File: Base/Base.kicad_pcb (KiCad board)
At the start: 2 copper layers, 72.4 x 72.4 mm, 33 parts, among them J1 USB_C_Receptacle_USB2.0_16P, J10 JST_switch_1, J11 JST_switch_2, J12 Conn_touch_1, J13 Conn_touch_2, J2 JST_battery, J3 JST_header, J4 JST_speaker, J5 JST_debug_swd, J6 JST_debug_serial, J7 Conn_speaker_sd, J8 Conn_speaker_gain, J9 Conn_speaker_gnd, SW1 SW_power, U1 MCP73831-2-OT, U2 MAX98357A

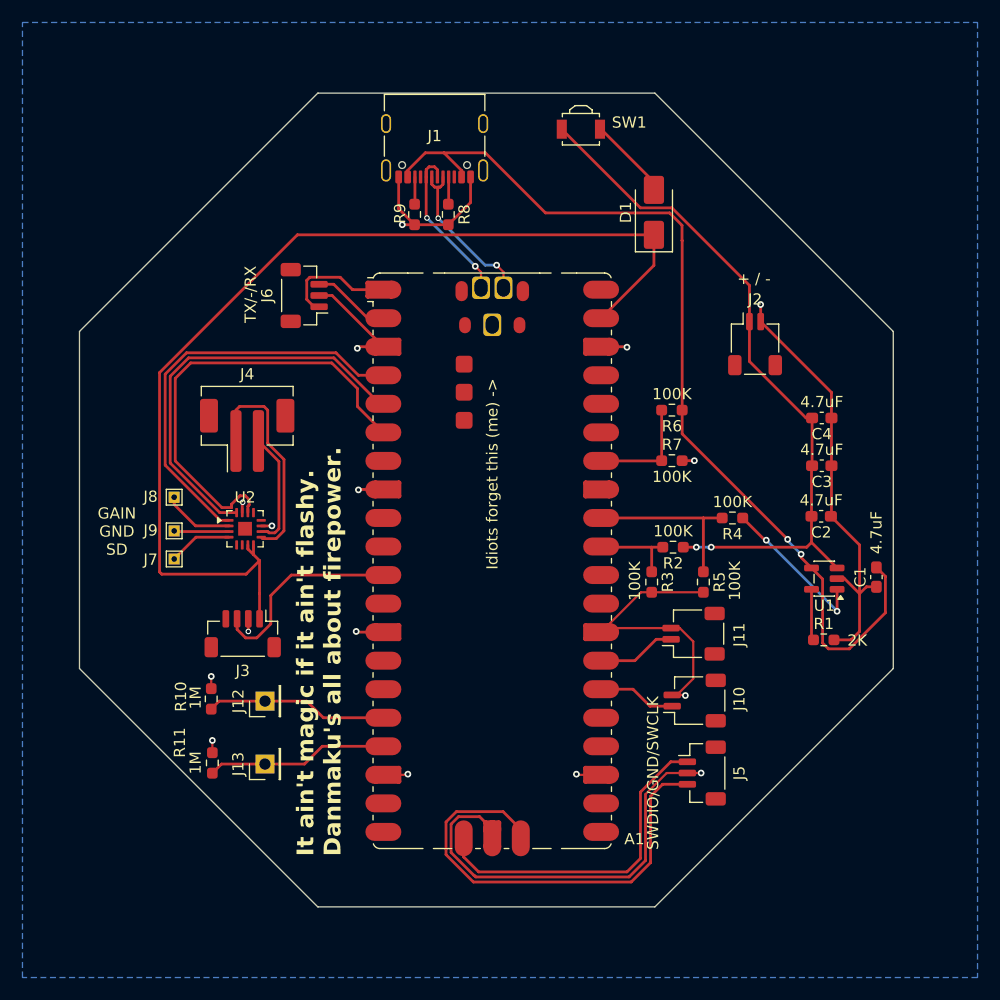
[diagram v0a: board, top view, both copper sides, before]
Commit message: Change switch to JST, fix polarity of battery connector, add power transistors for better LED off capability
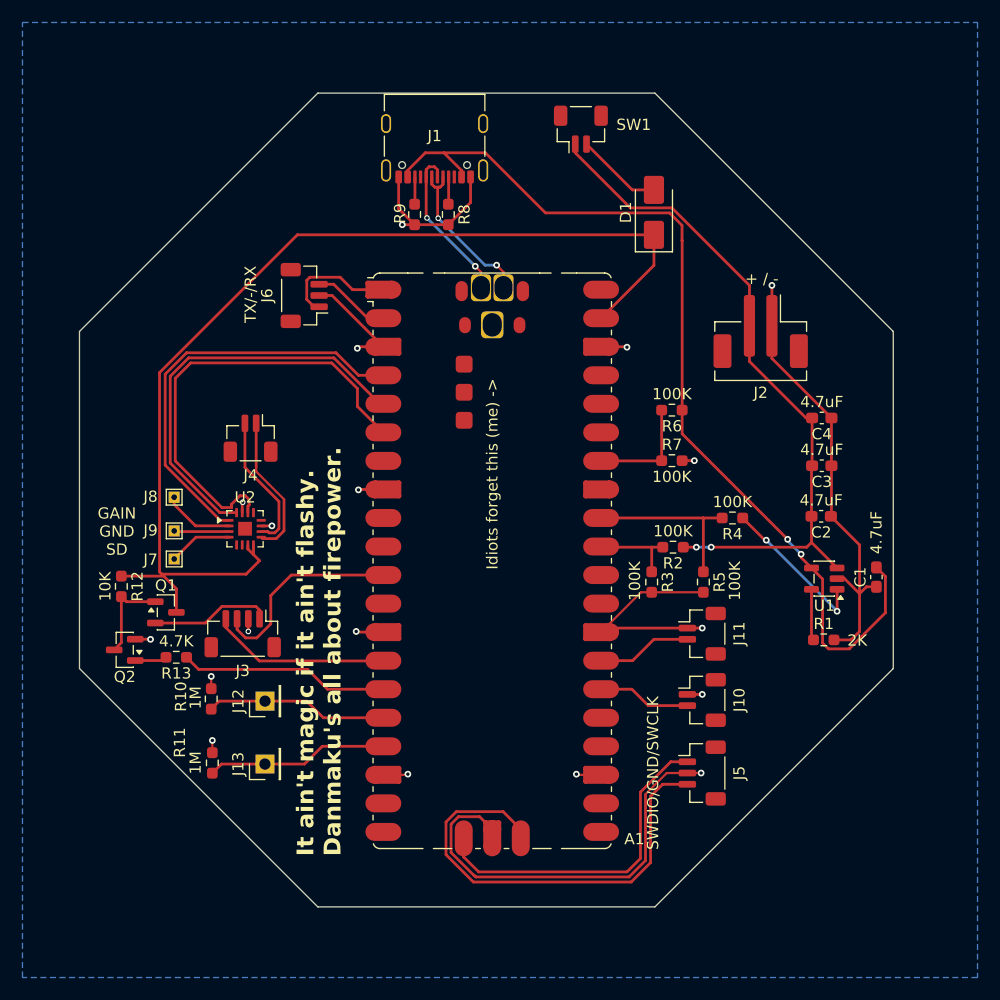
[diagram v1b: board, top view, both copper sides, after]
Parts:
- added Q1: AO3401A, Package_TO_SOT_SMD:SOT-23, F.Cu at (127.8, 112.5)
- added Q2: AO3400A, Package_TO_SOT_SMD:SOT-23, F.Cu at (124.1, 115.8)
- added R12: 10K, Resistor_SMD:R_0603_1608Metric_Pad0.98x0.95mm_HandSolder, F.Cu at (123.8, 110.2)
- added R13: 4.7K, Resistor_SMD:R_0603_1608Metric_Pad0.98x0.95mm_HandSolder, F.Cu at (128.7, 116.5)
- J10, J11: footprint Connector_JST:JST_SH_SM02B-SRSS-TB_1x02-1MP_P1.00mm_Horizontal -> Connector_JST:JST_SH_BM02B-SRSS-TB_1x02-1MP_P1.00mm_Vertical
- J2: footprint Connector_JST:JST_SH_SM02B-SRSS-TB_1x02-1MP_P1.00mm_Horizontal -> Connector_JST:JST_PH_B2B-PH-SM4-TB_1x02-1MP_P2.00mm_Vertical
- J4: footprint Connector_JST:JST_PH_B2B-PH-SM4-TB_1x02-1MP_P2.00mm_Vertical -> Connector_JST:JST_SH_BM02B-SRSS-TB_1x02-1MP_P1.00mm_Vertical
- SW1: footprint Button_Switch_SMD:SW_SPST_B3U-3000P -> Connector_JST:JST_SH_BM02B-SRSS-TB_1x02-1MP_P1.00mm_Vertical
- moved J2 1.23 mm to (180.7, 87.5), turned to 180 degrees
- moved J11 0.78 mm to (175.5, 114.4), turned to -90 degrees
- moved J10 0.68 mm to (175.5, 120.3), turned to -90 degrees
- moved J4 0.39 mm to (135.3, 97.0), turned to 180 degrees
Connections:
- A1 pad 13: /BAT_- -> GND
- A1 pad 14: unconnected-(A1-GPIO10-Pad14) -> /BUTTON_5
- A1 pad 15: unconnected-(A1-GPIO11-Pad15) -> /WS2812B_EN
- A1 pad 18: /BAT_- -> GND
- A1 pad 23: /BAT_- -> GND
- A1 pad 28: /BAT_- -> GND
- A1 pad 3: /BAT_- -> GND
- A1 pad 38: /BAT_- -> GND
- A1 pad 8: /BAT_- -> GND
- A1 pad D2: /BAT_- -> GND
- A1 pad TP1: /BAT_- -> GND
- C1 pad 1: /BAT_- -> GND
- C2 pad 1: /BAT_- -> GND
- C3 pad 1: /BAT_- -> GND
- C4 pad 1: /BAT_- -> GND
- J1 pad A1: /BAT_- -> GND
- J1 pad A12: /BAT_- -> GND
- J1 pad B1: /BAT_- -> GND
- J1 pad B12: /BAT_- -> GND
- J10 pad 1: /BUTTON_1 -> GND
- J10 pad 2: /BAT_- -> /BUTTON_1
- J11 pad 1: /BUTTON_2 -> GND
- J11 pad 2: /BAT_- -> /BUTTON_2
- J2 pad 1: /BAT_+ -> GND
- J2 pad 2: /BAT_- -> /BAT_+
- J3 pad 1: /SW_+ -> /WS2812B_VS
- J3 pad 2: /BAT_- -> GND
- J3 pad 4: unconnected-(J3-Pin_4-Pad4) -> /BUTTON_5
- J5 pad 2: /BAT_- -> GND
- J6 pad 2: /BAT_- -> GND
- J9 pad 1: /BAT_- -> GND
- R1 pad 2: /BAT_- -> GND
- R10 pad 2: /BAT_- -> GND
- R11 pad 2: /BAT_- -> GND
- R3 pad 2: /BAT_- -> GND
- R5 pad 2: /BAT_- -> GND
- R7 pad 2: /BAT_- -> GND
- R8 pad 2: /BAT_- -> GND
- R9 pad 2: /BAT_- -> GND
- U1 pad 2: /BAT_- -> GND
- U2 pad 11: /BAT_- -> GND
- U2 pad 15: /BAT_- -> GND
- U2 pad 3: /BAT_- -> GND
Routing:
- net /BAT_-: track 150.0 -> 0.00 mm, vias 16 -> 0
- net GND: track 0.00 -> 147.4 mm, vias 0 -> 18
- net /WS2812B_EN: track 0.00 -> 18.7 mm
- net /BUTTON_5: track 0.00 -> 16.0 mm
- net /WS2812B_VS: track 0.00 -> 10.8 mm
- net Net-(Q1-G): track 0.00 -> 8.21 mm
- net /SPEAKER_+: track 19.6 -> 13.0 mm
- net Net-(Q2-G): track 0.00 -> 2.86 mm
- net /SW_+: track 93.5 -> 96.1 mm
- net /SPEAKER_-: track 10.3 -> 12.4 mm
- net /BUTTON_2: track 7.01 -> 8.46 mm
- net /BUTTON_1: track 6.95 -> 8.28 mm
- net /BAT_+: track 62.9 -> 61.6 mm
- net Net-(D1-A): track 7.59 -> 8.39 mm
- added copper zone on B.Cu, net GND
- removed copper zone on B.Cu, net /BAT_-

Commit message: Add polarity solder jumpers for batteries that come in RNG polarity
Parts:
- added J14: Bat_pos_sel, Jumper:SolderJumper-3_P2.0mm_Open_TrianglePad1.0x1.5mm_NumberLabels, F.Cu at (177.2, 78.8)
- added J15: Bat_neg_sel, Jumper:SolderJumper-3_P2.0mm_Open_TrianglePad1.0x1.5mm_NumberLabels, F.Cu at (177.2, 82.8)
- moved J2 3.63 mm to (177.2, 88.5)
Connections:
- J2 pad 1: GND -> Net-(J14-Pin_3)
- J2 pad 2: /BAT_+ -> Net-(J14-Pin_1)
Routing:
- net GND: track 147.4 -> 136.1 mm, vias 18 -> 19
- net Net-(J14-Pin_3): track 0.00 -> 9.56 mm
- net Net-(J14-Pin_1): track 0.00 -> 9.56 mm
- net /BAT_+: track 61.6 -> 68.2 mm
- net /USB_VBUS: track 85.0 -> 89.6 mm
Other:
- board text added: "A / B"
- board text added: "MiniHakkero.EDA ${REVISION} (${VCSSHORTHASH}) By DoggySazHi"
- board text removed: "+ / -"
